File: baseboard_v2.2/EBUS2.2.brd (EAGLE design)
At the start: 62.8 x 59.4 mm, 51 parts, among them IC1 TLC393P, IC2 78L05Z

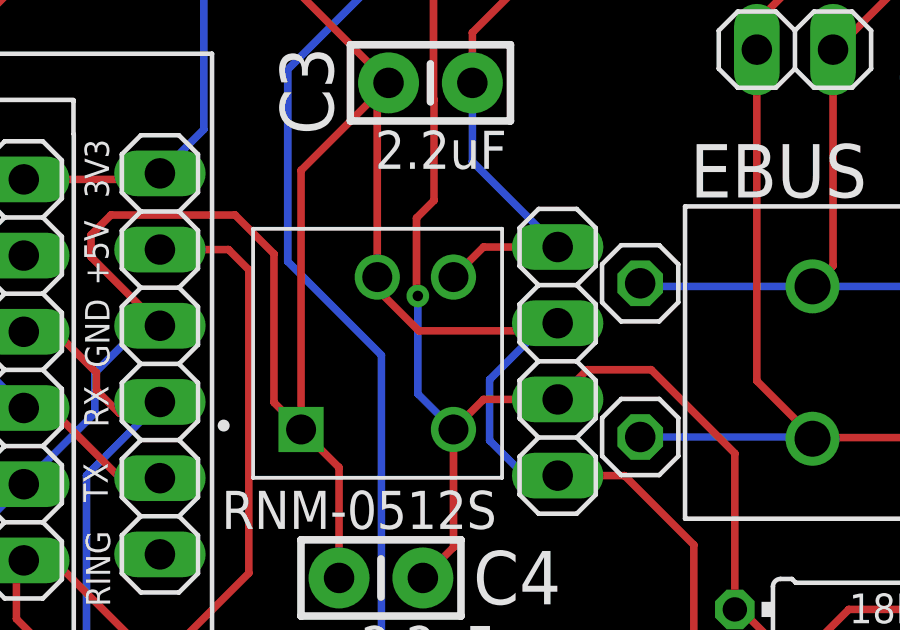
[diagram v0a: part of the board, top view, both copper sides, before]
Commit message: change external power pinout
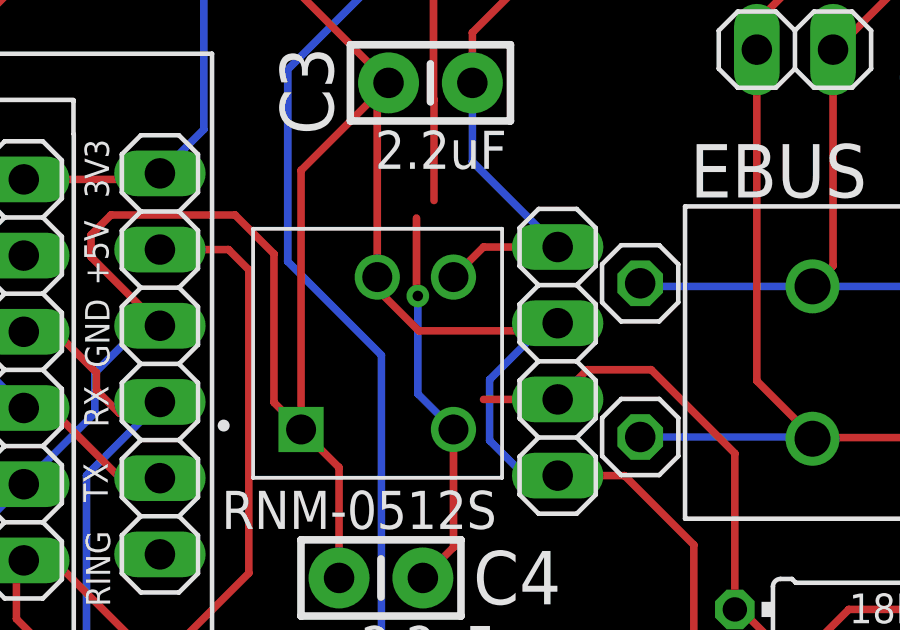
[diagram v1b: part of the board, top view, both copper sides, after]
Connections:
- net +5V: no longer C4.1, PS1.3
- net 5V: now also C4.1, PS1.3
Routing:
- net +5V: track 162.7 -> 147.5 mm, vias 2 -> 1
- net 5V: track 82.8 -> 95.8 mm, vias 2 -> 3
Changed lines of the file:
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@@
 <vertex x="99.187" y="85.217"/>
 </polygon>
+<contactref element="PS1" pad="3"/>
+<contactref element="C4" pad="1"/>
+<wire x1="139.634165625" y1="47.89671875" x2="140.654165625" y2="48.91671875" width="0.254" layer="1"/>
+<wire x1="140.654165625" y1="48.91671875" x2="140.654165625" y2="52.84583125" width="0.254" layer="1"/>
+<wire x1="139.4206" y1="59.8932" x2="139.4206" y2="57.3427" width="0.254" layer="1"/>
+<wire x1="139.4206" y1="57.3427" x2="139.46615" y2="57.29715" width="0.254" layer="1"/>
+<via x="139.46615" y="57.29715" extent="1-16" drill="0.35"/>
+<wire x1="139.46615" y1="57.29715" x2="139.46615" y2="54.033846875" width="0.254" layer="16"/>
+<wire x1="139.46615" y1="54.033846875" x2="140.654165625" y2="52.84583125" width="0.254" layer="16"/>
+<wire x1="130.8687875" y1="58.842459375" x2="139.4206" y2="59.8932" width="0" layer="19" extent="1-1"/>
 </signal>
 <signal name="RXI">
@@
 <contactref element="C2" pad="1"/>
 <contactref element="C1" pad="1"/>
-<contactref element="PS1" pad="3"/>
-<contactref element="C4" pad="1"/>
 <contactref element="JP4" pad="2"/>
 <wire x1="112.850084375" y1="84.881628125" x2="114.4016" y2="83.3301125" width="0.254" layer="1"/>
@@
 <wire x1="125.095" y1="69.0021875" x2="124.954584375" y2="69.142603125" width="0.254" layer="1"/>
 <wire x1="116.971740625" y1="66.2686" x2="123.7234" y2="66.2686" width="0.254" layer="1"/>
-<wire x1="140.654165625" y1="52.84583125" x2="141.655928125" y2="53.84759375" width="0.254" layer="1"/>
 <wire x1="141.655928125" y1="53.84759375" x2="144.127253125" y2="53.84759375" width="0.254" layer="1"/>
-<wire x1="139.634165625" y1="47.89671875" x2="140.654165625" y2="48.91671875" width="0.254" layer="1"/>
-<wire x1="140.654165625" y1="48.91671875" x2="140.654165625" y2="52.84583125" width="0.254" layer="1"/>
 <wire x1="148.781540625" y1="84.19223125" x2="145.1102" y2="80.520890625" width="0.254" layer="1"/>
 <wire x1="145.1102" y1="80.520890625" x2="145.1102" y2="77.724" width="0.254" layer="1"/>
@@
 <wire x1="137.26659375" y1="72.706246875" x2="139.9879" y2="69.984940625" width="0.254" layer="1"/>
 <wire x1="139.9879" y1="69.984940625" x2="139.9879" y2="63.86269375" width="0.254" layer="1"/>
-<wire x1="140.0048" y1="60.4774" x2="139.4206" y2="59.8932" width="0.254" layer="1"/>
-<wire x1="139.4206" y1="59.8932" x2="139.4206" y2="57.3427" width="0.254" layer="1"/>
-<wire x1="139.4206" y1="57.3427" x2="139.46615" y2="57.29715" width="0.254" layer="1"/>
-<via x="139.46615" y="57.29715" extent="1-16" drill="0.35"/>
-<wire x1="139.46615" y1="57.29715" x2="139.46615" y2="54.033846875" width="0.254" layer="16"/>
-<wire x1="139.46615" y1="54.033846875" x2="140.654165625" y2="52.84583125" width="0.254" layer="16"/>
 <wire x1="140.0048" y1="63.84579375" x2="140.0048" y2="60.4774" width="0.254" layer="1"/>
 <wire x1="144.127253125" y1="53.84759375" x2="145.118259375" y2="54.8386" width="0.254" layer="1"/>
@@
 <wire x1="150.02375" y1="41.81975" x2="150.17885" y2="41.81975" width="0.254" layer="1"/>
 <wire x1="148.717" y1="40.513" x2="150.02375" y2="41.81975" width="0.254" layer="1"/>
+<wire x1="140.0048" y1="60.4774" x2="141.655928125" y2="53.84759375" width="0" layer="19" extent="1-1"/>
 </signal>
 <signal name="N$4">

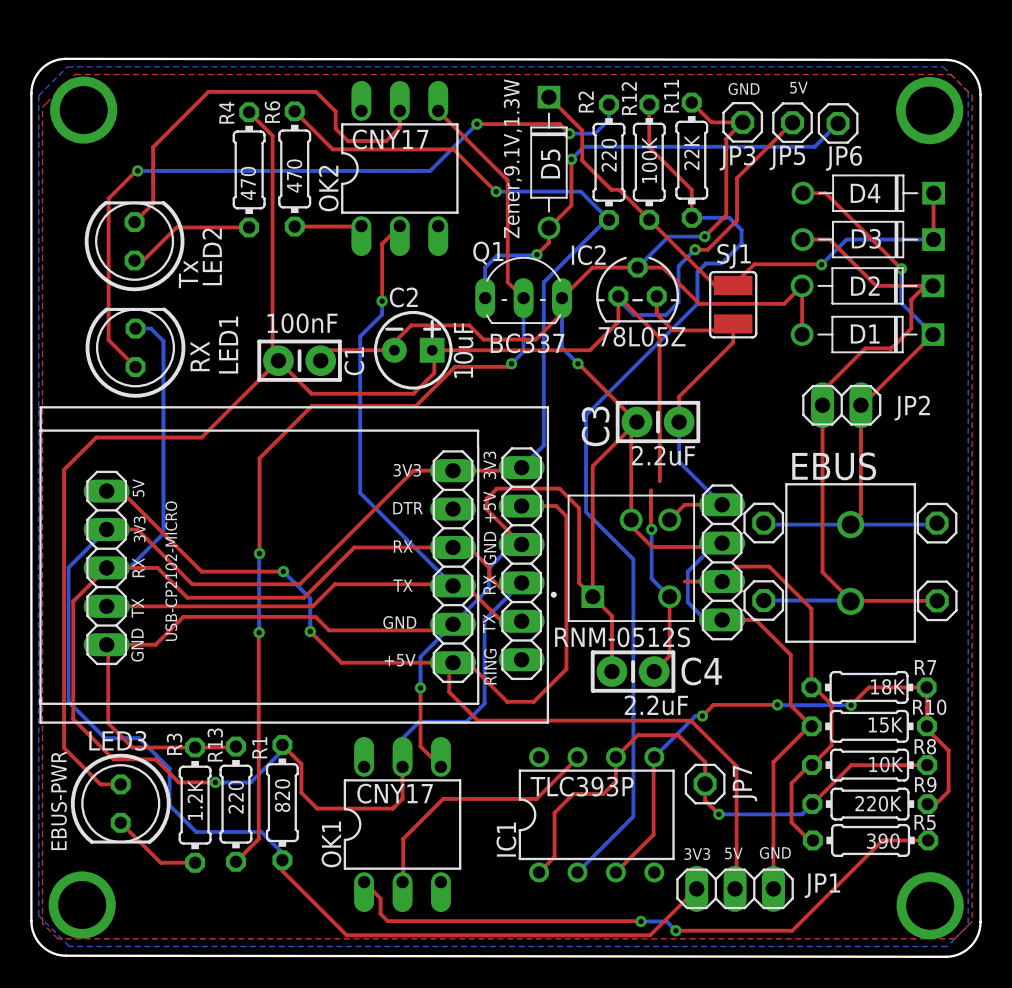
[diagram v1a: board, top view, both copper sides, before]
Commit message: Fix TLC389P powering
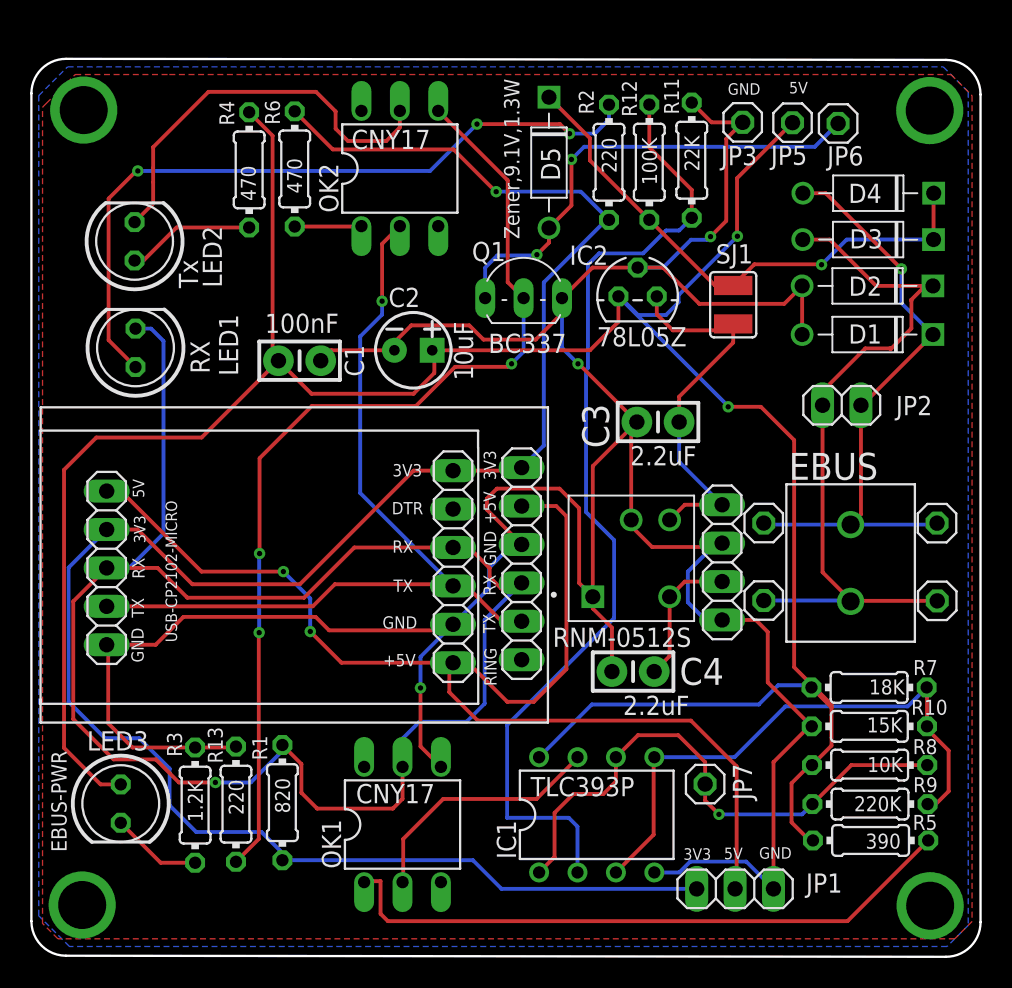
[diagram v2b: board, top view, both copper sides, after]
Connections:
- removed net V+: IC1.8
- removed net V-: IC1.4
- new net VCC: C4.1, JP4.2, PS1.3
- net +5V: now also IC1.8; no longer JP4.2
- net 5V: no longer C4.1, PS1.3
- net GND: now also IC1.4
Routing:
- net +5V: track 147.5 -> 172.8 mm, vias 1 -> 2
- net 5V: track 95.8 -> 82.8 mm, vias 3 -> 2
- net GND: track 205.3 -> 214.8 mm
- net VCC: track 0.00 -> 9.26 mm
- net +3V3: track 138.5 -> 135.5 mm
- net N$7: track 62.5 -> 65.1 mm
- net N$6: track 41.7 -> 41.9 mm, vias 2 -> 0
- net N$10: vias 3 -> 0
